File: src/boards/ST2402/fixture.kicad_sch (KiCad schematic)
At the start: 26 parts, among them J11 Conn_02x02_Top_Bottom, J12 Conn_02x02_Top_Bottom, J13 BNC, J14 Screw_Terminal_01x01, J18 Screw_Terminal_01x01, J19 BNC, J21 Conn_02x03_Top_Bottom, J22 Conn_02x03_Top_Bottom

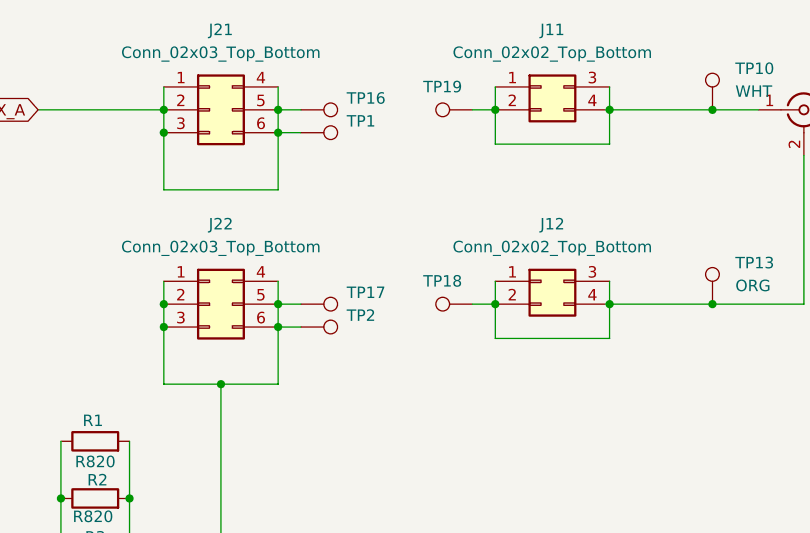
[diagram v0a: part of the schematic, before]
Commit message: Added Mouser part numbers
Updated BOM and schematic with Mouser part numbers
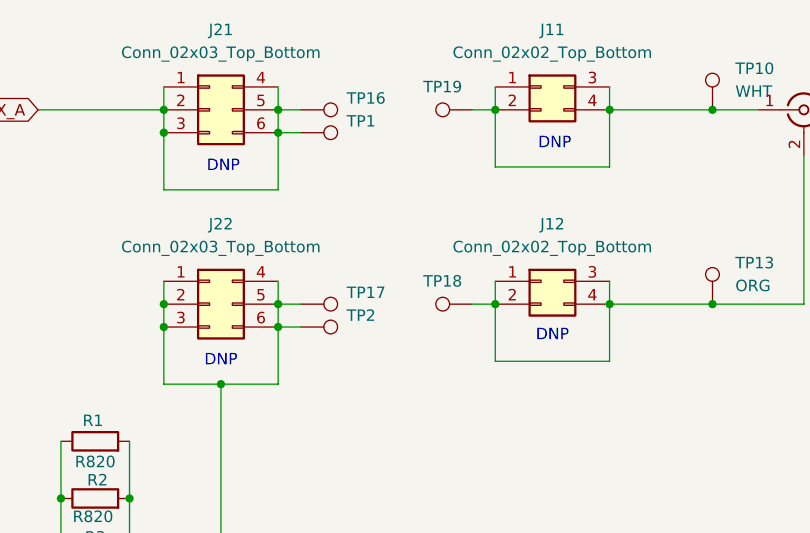
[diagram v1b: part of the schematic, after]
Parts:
- J11, J12: Mouser ordercode (none) -> 200-SSQ10203FD
- J13, J19: Mouser ordercode (none) -> 571-227661-1
- J14, J18: Mouser ordercode (none) -> ---
- J21, J22: Mouser ordercode (none) -> 200-SSQ10301GD
- R1, R2, R3, R4, R5, R6, R7, R8: Mouser ordercode (none) -> 71-RCWE1206R820FKEA
- TP1, TP2: Mouser ordercode (none) -> 510-CT4397-08-2
- TP10, TP14: Mouser ordercode (none) -> 534-5012
- TP13, TP15: Mouser ordercode (none) -> 534-5013
- TP16, TP17, TP18, TP19: Mouser ordercode (none) -> 706-02-0
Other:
- note added: "DNP"
